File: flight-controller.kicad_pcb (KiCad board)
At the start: 2 copper layers, 51 x 54 mm, 32 parts, among them J1 XT60PW-M, J2 Conn_01x04, J3 XT60PW-F, J4 XT60PW-F, J5 XT60PW-F, J6 XT60PW-F, U1 ACS773LCB-100B-PFF, U2 LMR33630ADDA, U3 AMS1117-3.3

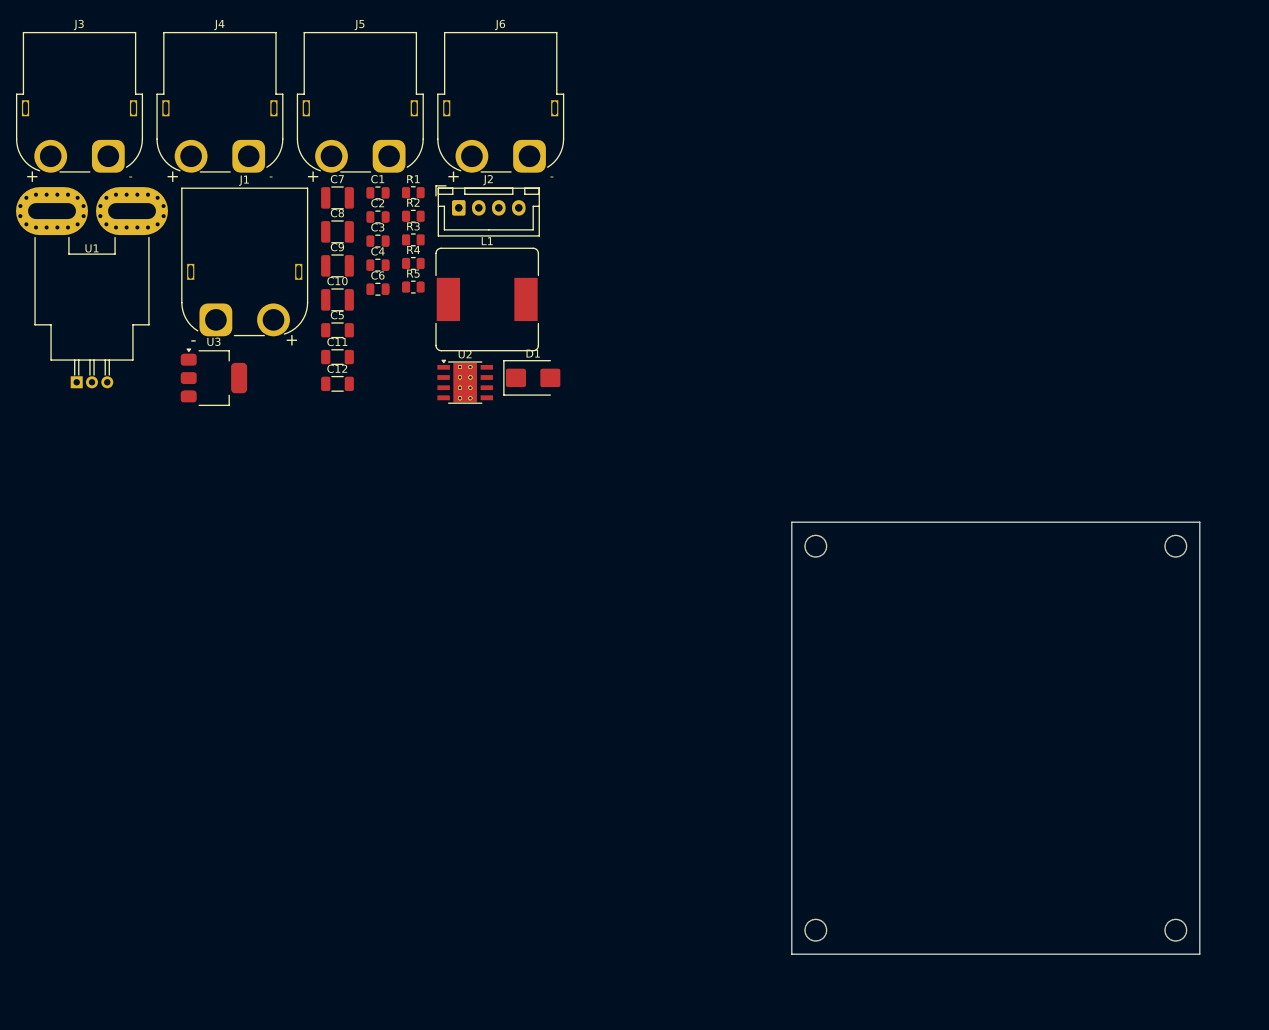
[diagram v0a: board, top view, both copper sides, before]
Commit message: fix: Updated right footprint and pcb design
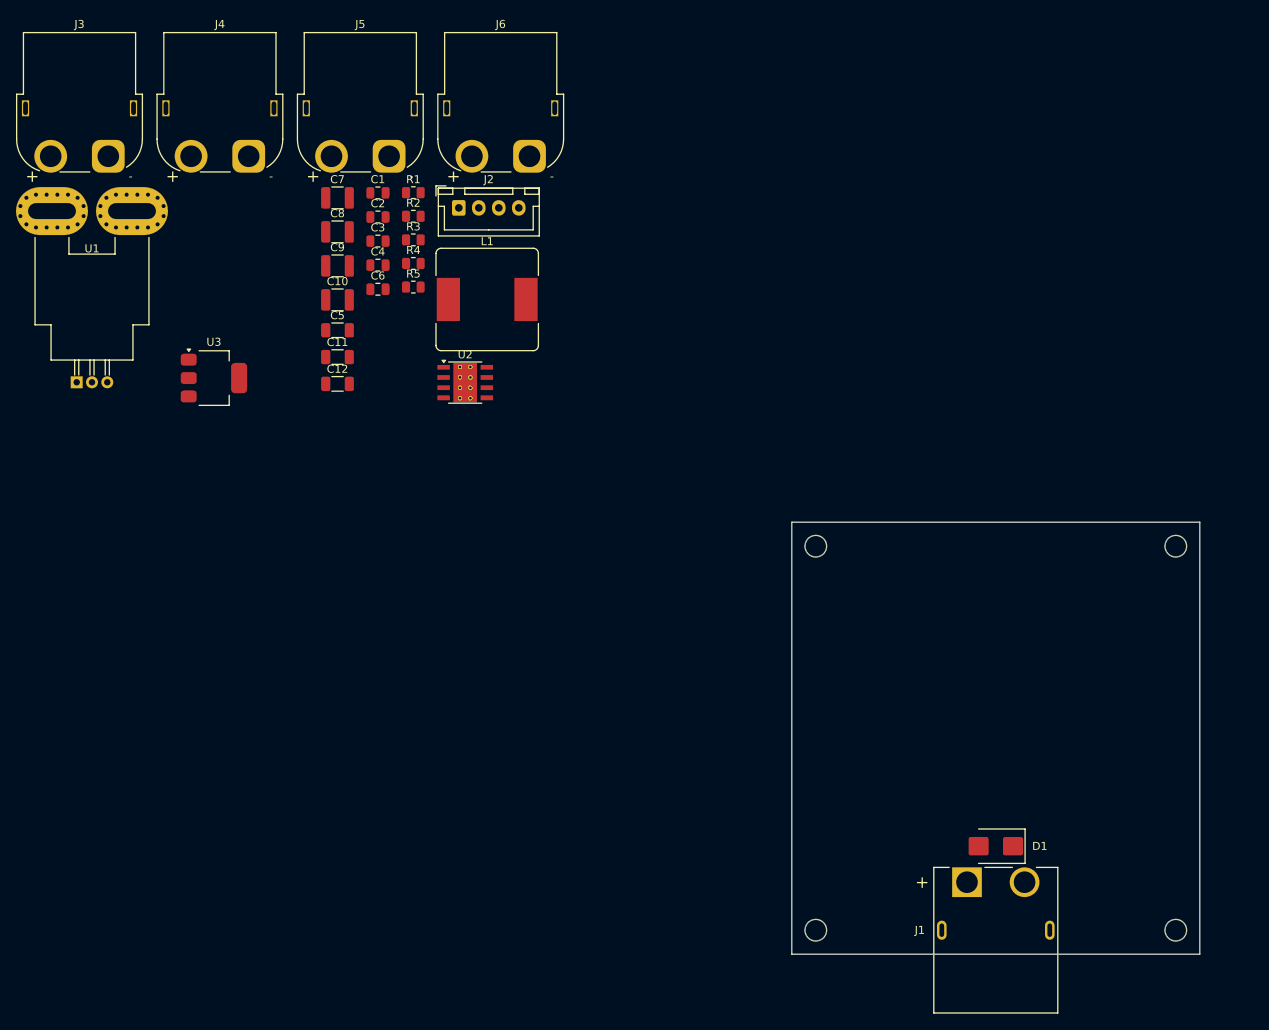
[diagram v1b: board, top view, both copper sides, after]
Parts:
- J1: footprint Connector_AMASS:AMASS_XT60PW-M_1x02_P7.20mm_Horizontal -> Custom_BEC_PS:AMASS_XT60PW-M
- moved J1 123.8 mm to (139.5, 130.0)
- moved D1 82.3 mm to (139.5, 119.5), turned to 180 degrees
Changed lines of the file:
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@@
   (net 12 "Net-(U2-FB)")
   (net 13 "unconnected-(U2-PG-Pad4)")
-  (footprint "Connector_AMASS:AMASS_XT60PW-M_1x02_P7.20mm_Horizontal" (layer "F.Cu")
-    (at 42.015 53.71)
-    (descr "Connector XT60 Horizontal PCB Female, https://www.tme.eu/en/Document/9b8d0c5eb7094295f3d3112c214d3ade/XT60PW%20SPEC.pdf")
-    (tags "RC Connector XT60")
+  (net 14 "unconnected-(J1-SHIELD-PadSH1)")
+  (footprint "Custom_BEC_PS:AMASS_XT60PW-M" (layer "F.Cu")
+    (at 139.5 130)
     (property "Availability" "In Stock")
     (property "CREATOR" "KARTHIK")
@@
     (property "SnapEDA_Link" "https://www.snapeda.com/parts/XT60PW-M/AMASS/view-part/?ref=snap")
     (attr through_hole)
-    (fp_text reference "J1" (at 3.6 -17.5) (layer "F.SilkS")
-        (effects (font (size 1 1) (thickness 0.15)))
-    )
-    (fp_text value "XT60PW-M" (at 3.6 4) (layer "F.Fab")
-        (effects (font (size 1 1) (thickness 0.15)))
-    )
-    (fp_text user "-" (at -2.8 2.5) (layer "F.SilkS")
-        (effects (font (size 1.5 1.5) (thickness 0.15)))
-    )
-    (fp_text user "+" (at 9.5 2.5) (layer "F.SilkS")
-        (effects (font (size 1.5 1.5) (thickness 0.15)))
-    )
-    (fp_text user "${REFERENCE}" (at 3.6 -3.6) (layer "F.Fab")
-        (effects (font (size 1 1) (thickness 0.15)))
-    )
-    (fp_line (start -4.26 -16.46) (end -4.26 -2.15)
-      (stroke (width 0.12) (type solid)) (layer "F.SilkS"))
-    (fp_line (start -4.26 -16.46) (end 11.46 -16.46)
-      (stroke (width 0.12) (type solid)) (layer "F.SilkS"))
-    (fp_line (start 2.31 1.96) (end 6.05 1.96)
-      (stroke (width 0.12) (type solid)) (layer "F.SilkS"))
-    (fp_line (start 11.46 -16.46) (end 11.46 -2.15)
-      (stroke (width 0.12) (type solid)) (layer "F.SilkS"))
-    (fp_arc (start -2.266806 1.372958) (mid -3.727162 -0.126139) (end -4.26 -2.15)
-      (stroke (width 0.12) (type solid)) (layer "F.SilkS"))
-    (fp_arc (start 11.46 -2.15) (mid 10.653852 0.294722) (end 8.551648 1.780413)
-      (stroke (width 0.12) (type solid)) (layer "F.SilkS"))
-    (fp_line (start -4.65 -16.85) (end -4.65 2.55)
-      (stroke (width 0.05) (type solid)) (layer "F.CrtYd"))
-    (fp_line (start -4.65 -16.85) (end 11.85 -16.85)
-      (stroke (width 0.05) (type solid)) (layer "F.CrtYd"))
-    (fp_line (start 11.85 -16.85) (end 11.85 2.55)
-      (stroke (width 0.05) (type solid)) (layer "F.CrtYd"))
-    (fp_line (start 11.85 2.55) (end -4.65 2.55)
-      (stroke (width 0.05) (type solid)) (layer "F.CrtYd"))
-    (fp_line (start -4.15 -16.35) (end -4.15 -2.15)
-      (stroke (width 0.1) (type solid)) (layer "F.Fab"))
-    (fp_line (start -4.15 -16.35) (end 11.35 -16.35)
-      (stroke (width 0.1) (type solid)) (layer "F.Fab"))
-    (fp_line (start -0.15 1.85) (end 7.35 1.85)
-      (stroke (width 0.1) (type solid)) (layer "F.Fab"))
-    (fp_line (start 11.35 -16.35) (end 11.35 -2.15)
-      (stroke (width 0.1) (type solid)) (layer "F.Fab"))
-    (fp_arc (start -0.15 1.85) (mid -2.978427 0.678427) (end -4.15 -2.15)
-      (stroke (width 0.1) (type solid)) (layer "F.Fab"))
-    (fp_arc (start 11.35 -2.15) (mid 10.178427 0.678427) (end 7.35 1.85)
-      (stroke (width 0.1) (type solid)) (layer "F.Fab"))
-    (pad "" thru_hole rect (at -3.15 -6) (size 0.9 2) (drill oval 0.6 1.7) (layers "*.Cu" "*.Mask"))
-    (pad "" thru_hole rect (at 10.35 -6) (size 0.9 2) (drill oval 0.6 1.7) (layers "*.Cu" "*.Mask"))
-    (pad "1" thru_hole roundrect (at 0 0) (size 4.1 4.1) (drill 2.7) (layers "*.Cu" "*.Mask") (roundrect_rratio 0.25)
-      (net 7 "/VBAT") (pinfunction "P") (pintype "passive"))
-    (pad "2" thru_hole circle (at 7.2 0) (size 4.1 4.1) (drill 2.7) (layers "*.Cu" "*.Mask")
-      (net 2 "GND") (pinfunction "N") (pintype "passive"))
-    (model "${KICAD6_3DMODEL_DIR}/Connector_AMASS.3dshapes/AMASS_XT60PW-M_1x02_P7.20mm_Horizontal.wrl"
-      (offset (xyz 0 0 0))
-      (scale (xyz 1 1 1))
-      (rotate (xyz 0 0 0))
+    (fp_text reference "J1" (at -9.5 0) (layer "F.SilkS")
+        (effects (font (size 1.000441 1.000441) (thickness 0.15)))
+    )
+    (fp_text value "XT60PW-M" (at 1.0054 -9.4434) (layer "F.Fab")
+        (effects (font (size 1.001732 1.001732) (thickness 0.15)))
+    )
+    (fp_line (start -9.8 -5.95) (end -8.6 -5.95)
+      (stroke (width 0.127) (type solid)) (layer "F.SilkS"))
+    (fp_line (start -9.2 -6.55) (end -9.2 -5.35)
+      (stroke (width 0.127) (type solid)) (layer "F.SilkS"))
+    (fp_line (start -7.75 -7.85) (end -7.75 10.35)
+      (stroke (width 0.127) (type solid)) (layer "F.SilkS"))
+    (fp_line (start -7.75 -7.85) (end -5.828 -7.85)
+      (stroke (width 0.127) (type solid)) (layer "F.SilkS"))
+    (fp_line (start -7.75 10.35) (end 7.75 10.35)
+      (stroke (width 0.127) (type solid)) (layer "F.SilkS"))
+    (fp_line (start 2.072 -7.85) (end -1.372 -7.85)
+      (stroke (width 0.127) (type solid)) (layer "F.SilkS"))
+    (fp_line (start 7.75 -7.85) (end 5.078 -7.85)
+      (stroke (width 0.127) (type solid)) (layer "F.SilkS"))
+    (fp_line (start 7.75 10.35) (end 7.75 -7.85)
+      (stroke (width 0.127) (type solid)) (layer "F.SilkS"))
+    (fp_line (start -8 -8.11) (end -8 10.6)
+      (stroke (width 0.05) (type solid)) (layer "F.CrtYd"))
+    (fp_line (start -8 10.6) (end 8 10.6)
+      (stroke (width 0.05) (type solid)) (layer "F.CrtYd"))
+    (fp_line (start 8 -8.11) (end -8 -8.11)
+      (stroke (width 0.05) (type solid)) (layer "F.CrtYd"))
+    (fp_line (start 8 10.6) (end 8 -8.11)
+      (stroke (width 0.05) (type solid)) (layer "F.CrtYd"))
+    (fp_line (start -9.8 -5.95) (end -8.6 -5.95)
+      (stroke (width 0.127) (type solid)) (layer "F.Fab"))
+    (fp_line (start -9.2 -6.55) (end -9.2 -5.35)
+      (stroke (width 0.127) (type solid)) (layer "F.Fab"))
+    (fp_line (start -7.75 -7.85) (end -7.75 10.35)
+      (stroke (width 0.127) (type solid)) (layer "F.Fab"))
+    (fp_line (start -7.75 10.35) (end 7.75 10.35)
+      (stroke (width 0.127) (type solid)) (layer "F.Fab"))
+    (fp_line (start 7.75 -7.85) (end -7.75 -7.85)
+      (stroke (width 0.127) (type solid)) (layer "F.Fab"))
+    (fp_line (start 7.75 10.35) (end 7.75 -7.85)
+      (stroke (width 0.127) (type solid)) (layer "F.Fab"))
+    (pad "1" thru_hole rect (at -3.6 -6) (size 3.716 3.716) (drill 2.7) (layers "*.Cu" "*.Mask")
+      (net 7 "/VBAT") (pinfunction "P") (pintype "passive") (solder_mask_margin 0.102))
+    (pad "2" thru_hole circle (at 3.6 -6) (size 3.716 3.716) (drill 2.7) (layers "*.Cu" "*.Mask")
+      (net 2 "GND") (pinfunction "N") (pintype "passive") (solder_mask_margin 0.102))
+    (pad "SH1" thru_hole oval (at -6.75 0) (size 1.2 2.4) (drill oval 0.6 1.7) (layers "*.Cu" "*.Mask")
+      (net 14 "unconnected-(J1-SHIELD-PadSH1)") (pinfunction "SHIELD") (pintype "passive+no_connect") (solder_mask_margin 0.102))
+    (pad "SH2" thru_hole oval (at 6.75 0) (size 1.2 2.4) (drill oval 0.6 1.7) (layers "*.Cu" "*.Mask")
+      (net 14 "unconnected-(J1-SHIELD-PadSH1)") (pinfunction "SHIELD") (pintype "passive+no_connect") (solder_mask_margin 0.102))
+    (model "${KIPRJMOD}/lib/3d_models/XT60PW-M.step"
+      (offset (xyz 0 0 0))
+      (scale (xyz 1 1 1))
+      (rotate (xyz -90 0 0))
     )
   )
@@
   )
   (footprint "Diode_SMD:D_SMB" (layer "F.Cu")
-    (at 81.67 60.96)
+    (at 139.5 119.5 180)
     (descr "Diode SMB (DO-214AA)")
     (tags "Diode SMB (DO-214AA)")
@@
     (property "ki_keywords" "diode")
     (attr smd)
-    (fp_text reference "D1" (at 0 -3) (layer "F.SilkS")
+    (fp_text reference "D1" (at -5.5 0) (layer "F.SilkS")
         (effects (font (size 1 1) (thickness 0.15)))
     )
@@
         (effects (font (size 1 1) (thickness 0.15)))
     )
-    (fp_text user "${REFERENCE}" (at 0 -3) (layer "F.Fab")
+    (fp_text user "${REFERENCE}" (at -5.5 2) (layer "F.Fab")
         (effects (font (size 1 1) (thickness 0.15)))
     )
@@
     (fp_line (start 2.3 2) (end -2.3 2)
       (stroke (width 0.1) (type solid)) (layer "F.Fab"))
-    (pad "1" smd roundrect (at -2.15 0) (size 2.5 2.3) (layers "F.Cu" "F.Paste" "F.Mask") (roundrect_rratio 0.1086956522)
+    (pad "1" smd roundrect (at -2.15 0 180) (size 2.5 2.3) (layers "F.Cu" "F.Paste" "F.Mask") (roundrect_rratio 0.1086956522)
       (net 7 "/VBAT") (pinfunction "K") (pintype "passive"))
-    (pad "2" smd roundrect (at 2.15 0) (size 2.5 2.3) (layers "F.Cu" "F.Paste" "F.Mask") (roundrect_rratio 0.1086956522)
+    (pad "2" smd roundrect (at 2.15 0 180) (size 2.5 2.3) (layers "F.Cu" "F.Paste" "F.Mask") (roundrect_rratio 0.1086956522)
       (net 2 "GND") (pinfunction "A") (pintype "passive"))
     (model "${KICAD6_3DMODEL_DIR}/Diode_SMD.3dshapes/D_SMB.wrl"

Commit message: feat: Updated schematic and pcb to use correct xt60 3d model
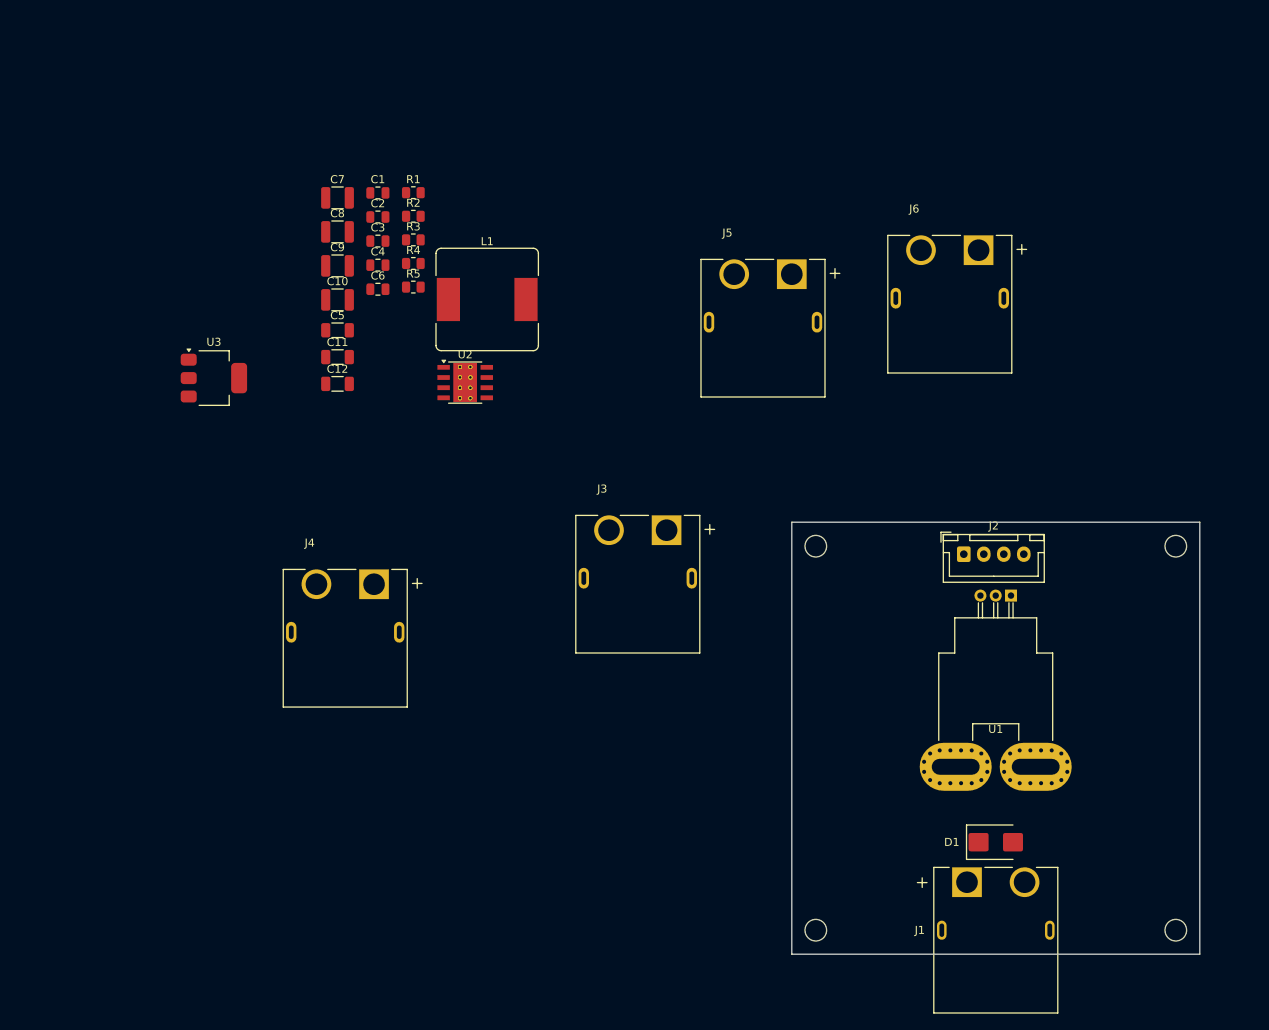
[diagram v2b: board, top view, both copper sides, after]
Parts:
- J3, J4, J5, J6: footprint Connector_AMASS:AMASS_XT60PW-F_1x02_P7.20mm_Horizontal -> Custom_BEC_PS:AMASS_XT60PW-F
- moved U1 119.8 mm to (141.4, 88.2), turned to 180 degrees
- moved J3 81.0 mm to (94.8, 80.0)
- moved J2 76.5 mm to (135.5, 83.0)
- moved J4 54.8 mm to (58.2, 86.8)
- moved J6 53.8 mm to (133.8, 45.0)
- moved J5 49.0 mm to (110.4, 48.0)
- moved D1 0.50 mm to (139.5, 119.0), turned to 0 degrees

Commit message: feat: Modified connector to flight controller from power board
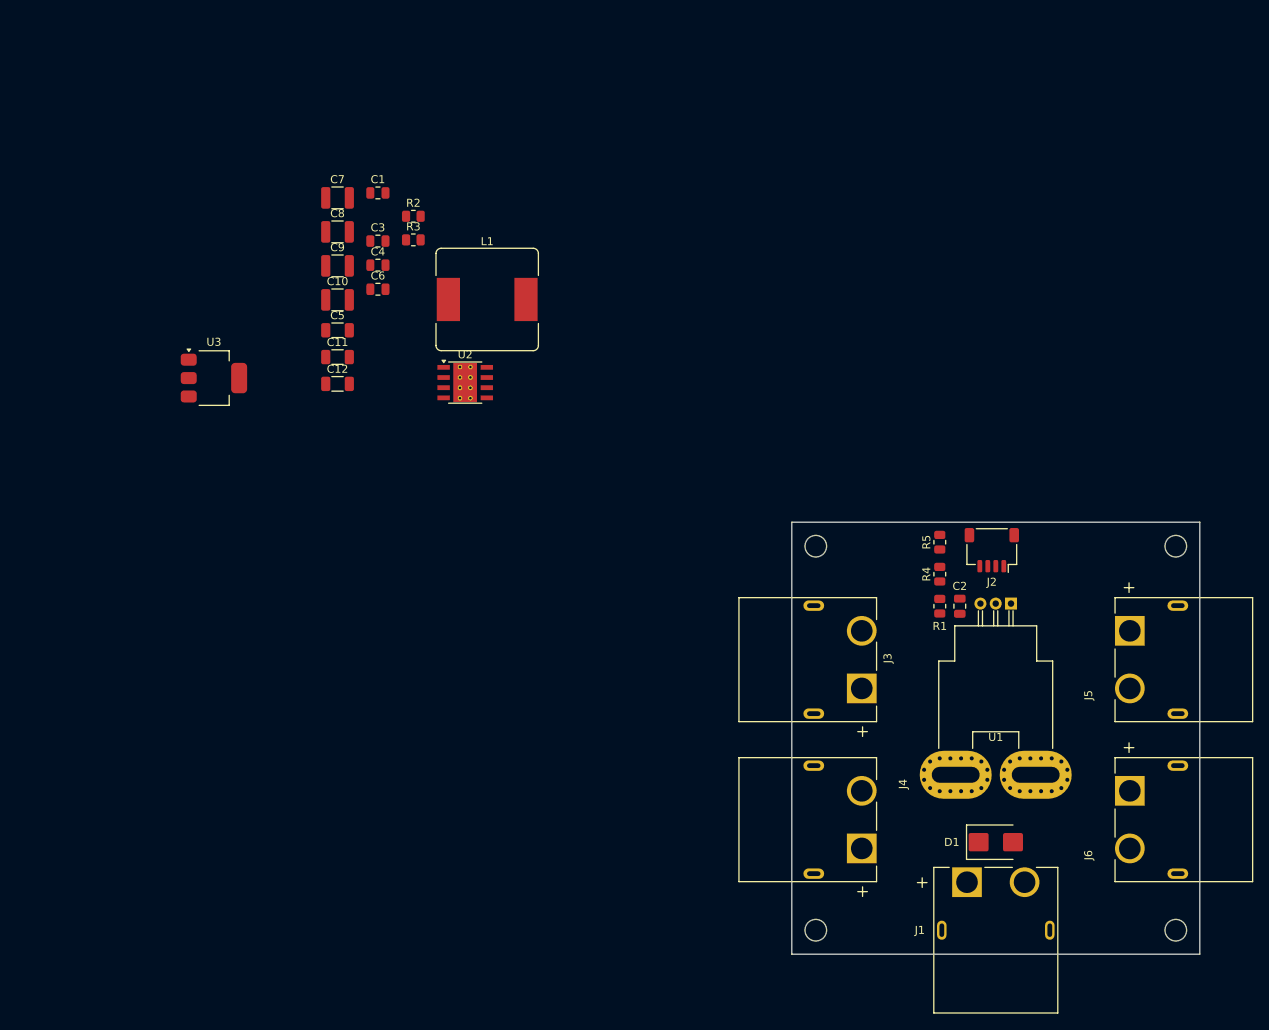
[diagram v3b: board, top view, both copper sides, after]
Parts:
- J2: value Conn_01x04 -> SM04B-SRSS-TB; footprint Connector_JST:JST_XH_B4B-XH-A_1x04_P2.50mm_Vertical -> Connector_JST:JST_SH_SM04B-SRSS-TB_1x04-1MP_P1.00mm_Horizontal
- moved C2 87.5 mm to (135.0, 89.5), turned to -90 degrees
- moved R1 83.7 mm to (132.5, 89.5), turned to -90 degrees
- moved R4 76.4 mm to (132.5, 85.5), turned to 90 degrees
- moved J6 74.7 mm to (156.3, 116.2), turned to 90 degrees
- moved R5 73.1 mm to (132.5, 81.5), turned to 90 degrees
- moved J4 71.0 mm to (122.7, 116.2), turned to -90 degrees
- moved J5 66.5 mm to (156.3, 96.2), turned to 90 degrees
- moved J3 32.3 mm to (122.7, 96.2), turned to -90 degrees
- moved J2 3.54 mm to (139.0, 82.5), turned to 180 degrees
- moved U1 1.00 mm to (141.4, 89.2)
